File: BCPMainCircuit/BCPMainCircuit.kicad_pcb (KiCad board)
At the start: 2 copper layers, 94 x 88 mm, 8 parts, among them SW1 SW_Nidec_CAS-120A1, U1 LD1117V33, U2 Pico 2, U3 DEV-13712, U6 BME280

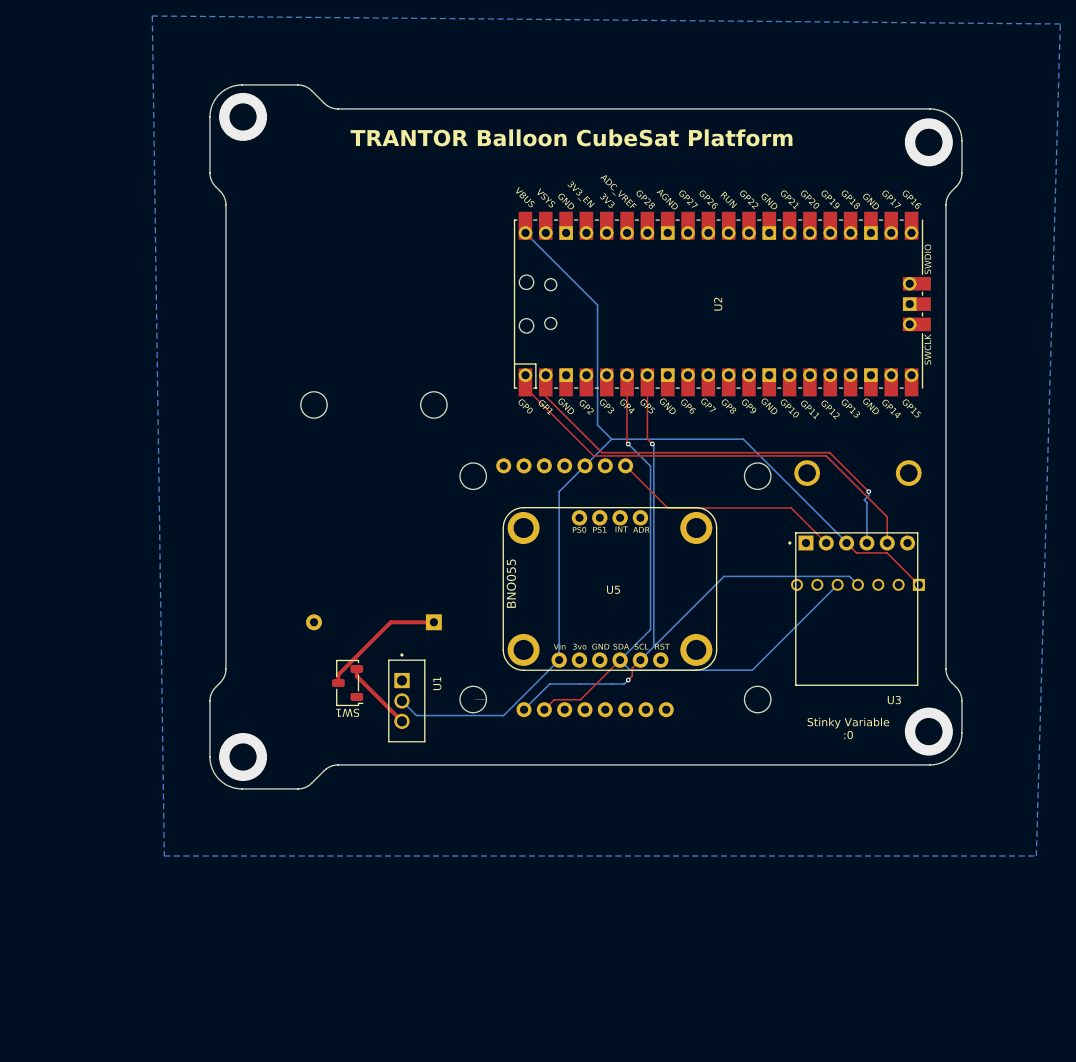
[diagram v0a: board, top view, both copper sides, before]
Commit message: Added a ground pour
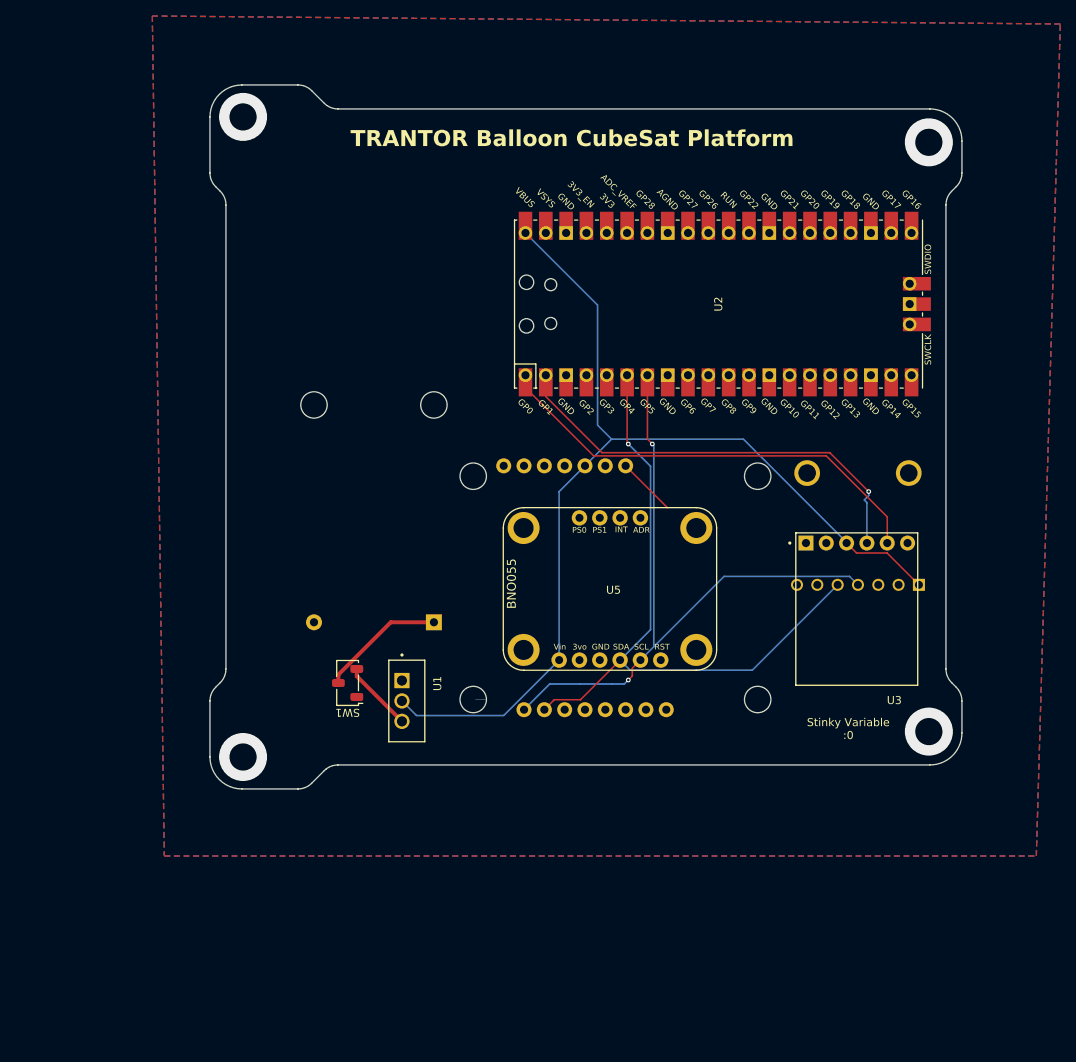
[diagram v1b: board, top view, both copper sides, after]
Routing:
- net GND: track 29.1 -> 7.45 mm
- added copper zone on F.Cu, net GND
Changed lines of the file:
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@@
-	)
-	(segment
-		(start 146.865 85)
-		(end 131.433372 85)
-		(width 0.2)
-		(layer "F.Cu")
-		(net 4)
 	)
 	(segment
 		(start 131.433372 85)
 		(end 126.162972 79.7296)
-		(width 0.2)
-		(layer "F.Cu")
-		(net 4)
-	)
-	(segment
-		(start 151.245 89.38)
-		(end 146.865 85)
 		(width 0.2)
 		(layer "F.Cu")
@@
 		(net 4)
 		(net_name "GND")
-		(layer "B.Cu")
+		(layers "F.Cu" "B.Cu")
 		(hatch edge 0.5)
 		(connect_pads

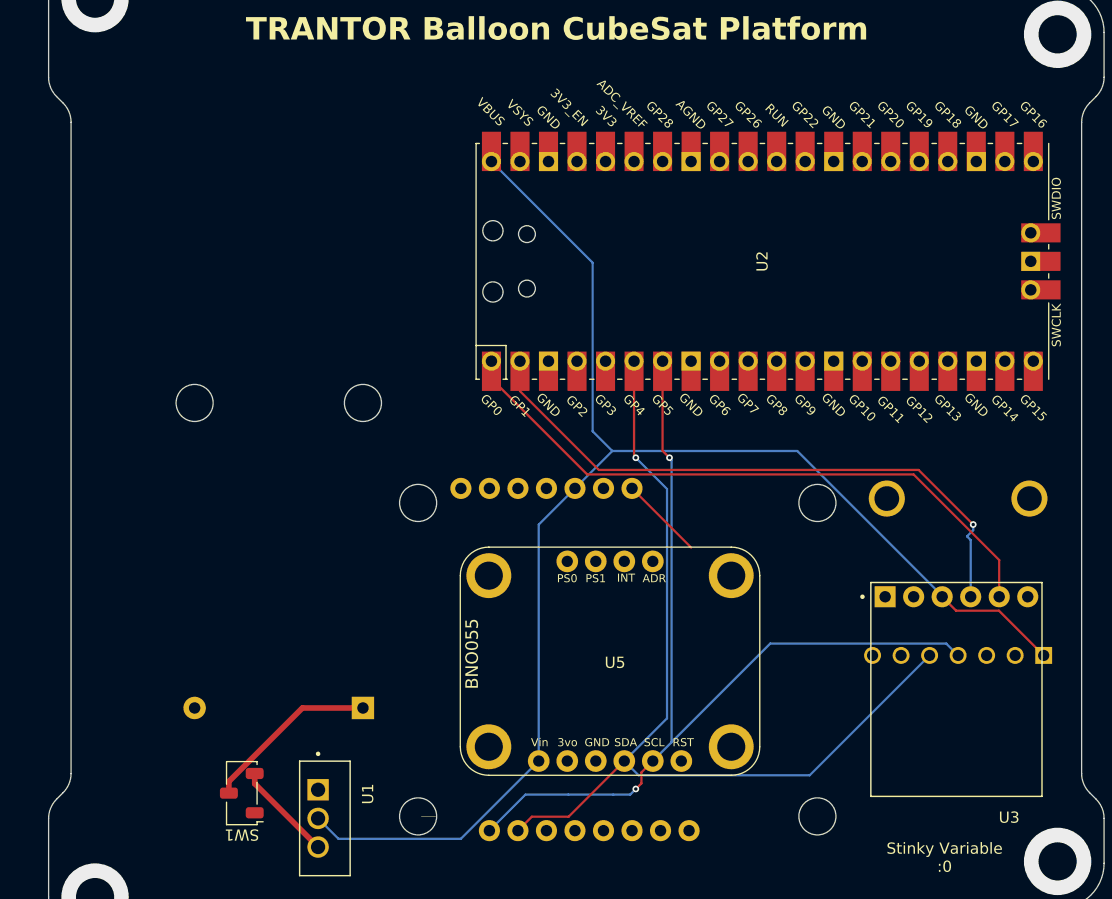
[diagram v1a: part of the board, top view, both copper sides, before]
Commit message: Fixed overlapping footprints
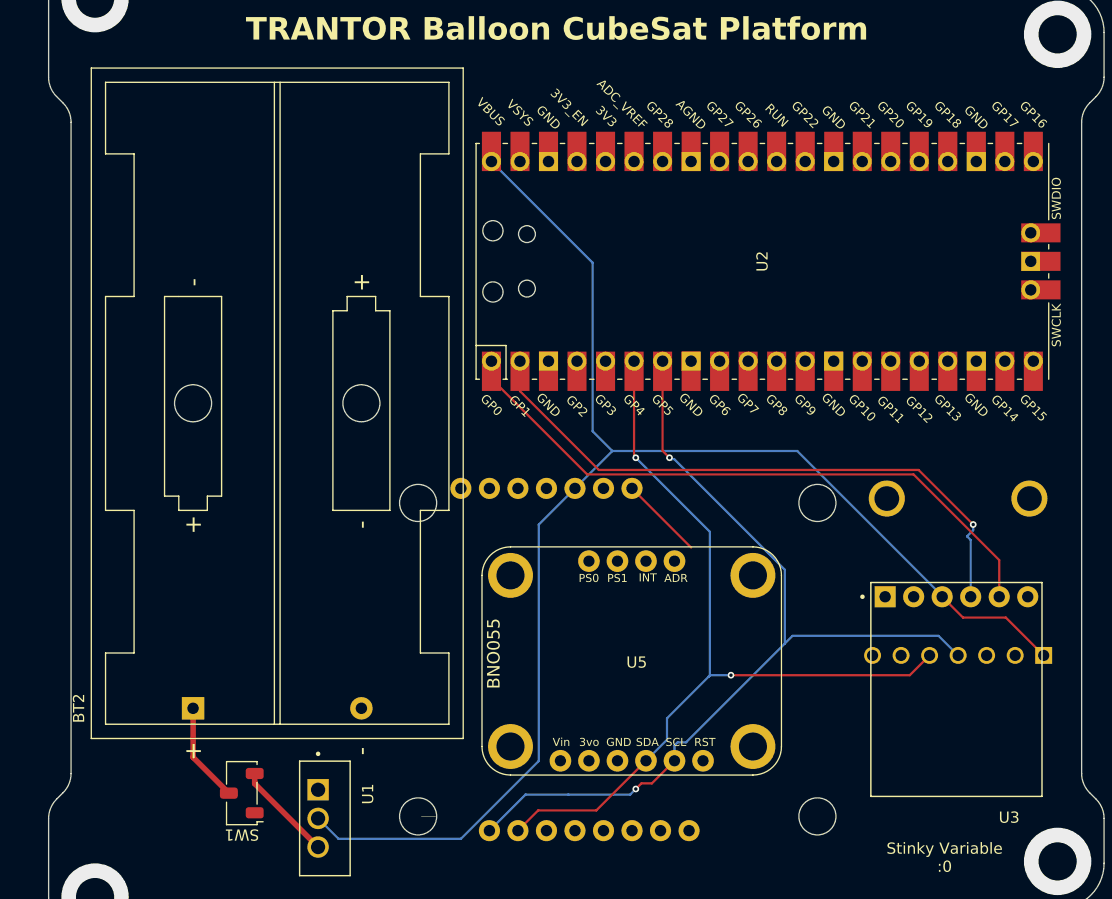
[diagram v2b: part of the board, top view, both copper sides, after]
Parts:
- BT2: moved to F.Cu
- moved BT2 15.1 mm to (87.1, 99.3)
- moved U5 1.93 mm to (126.6, 95.7)
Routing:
- net /SDA: track 82.6 -> 75.2 mm, vias 1 -> 2
- net Net-(BT2-+): track 15.7 -> 8.88 mm
- net /SCL: track 83.9 -> 80.2 mm

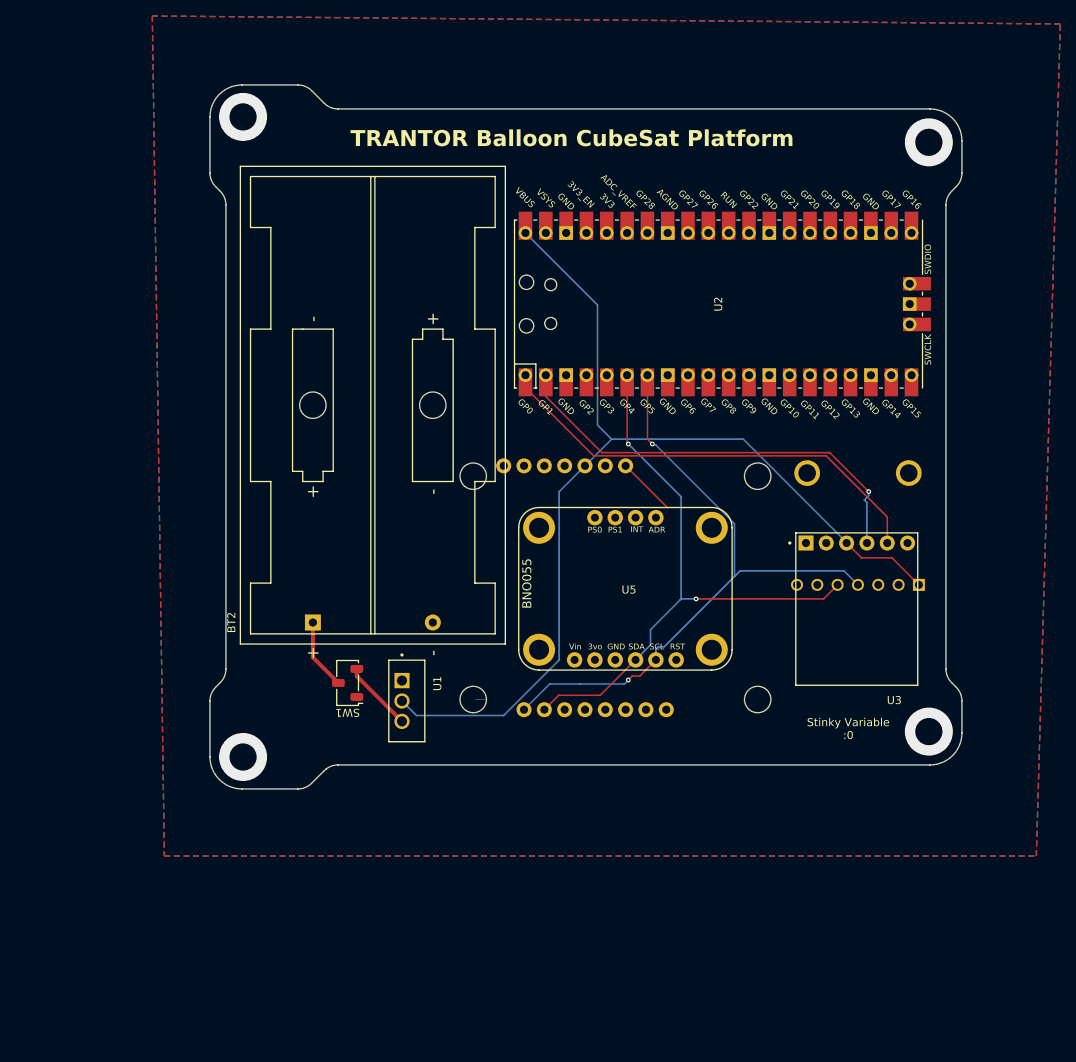
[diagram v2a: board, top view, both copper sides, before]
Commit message: Update LEDs and Silkscreen
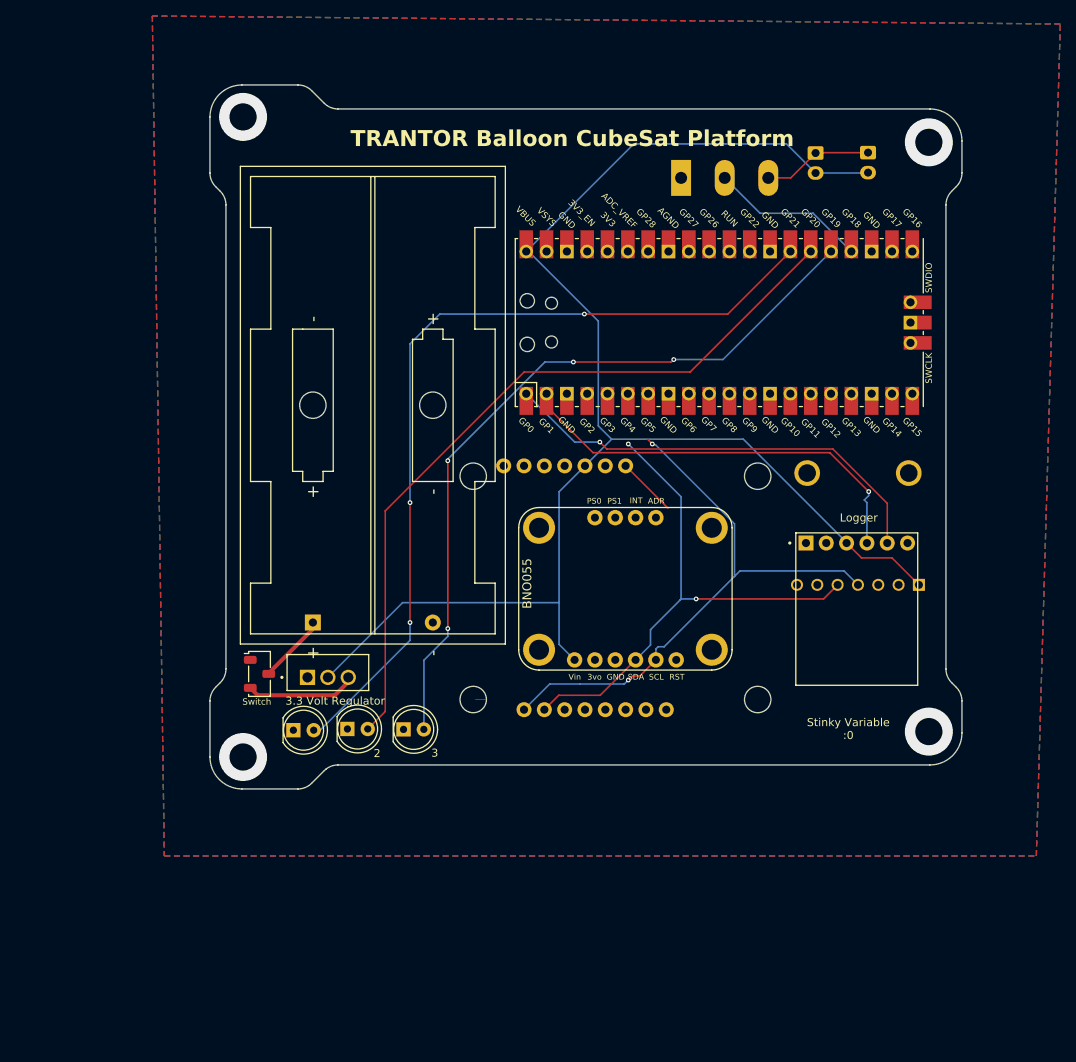
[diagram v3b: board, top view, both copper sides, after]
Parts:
- added D1: Flight LED 1, Connector_JST:JST_EH_B2B-EH-A_1x02_P2.50mm_Vertical, B.Cu at (156.5, 40.6)
- added D2: 1, LED_THT:LED_D5.0mm, F.Cu at (84.6, 112.8)
- added D3: 2, LED_THT:LED_D5.0mm, F.Cu at (91.4, 112.6)
- added D4: 3, LED_THT:LED_D5.0mm, F.Cu at (98.4, 112.7)
- added D5: Flight LED 2, Connector_JST:JST_EH_B2B-EH-A_1x02_P2.50mm_Vertical, B.Cu at (149.9, 40.6)
- added Mosfet: PMOS, Package_TO_SOT_THT:TO-247-3_Vertical, B.Cu at (133.1, 43.7)
- BT2: value Battery -> Batteries
- SW1: value SW_Nidec_CAS-120A1 -> Switch
- U1: value LD1117V33 -> 3.3 Volt Regulator
- U3: value DEV-13712 -> Logger
- U5: value ~ -> BNO055
- moved SW1 11.1 mm to (80.4, 105.7), turned to 0 degrees
- moved U1 10.5 mm to (88.9, 105.6), turned to 0 degrees
- moved U2 2.32 mm to (137.9, 61.8)
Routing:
- net /DEBUG1: track 0.00 -> 106.1 mm, vias 0 -> 3
- net /DEBUG2: track 0.00 -> 94.8 mm
- net /DEBUG3: track 0.00 -> 93.7 mm, vias 0 -> 4
- net /3.3 V: track 129.8 -> 187.9 mm
- net /FLIGHTLED: track 0.00 -> 19.6 mm
- net Net-(D1-K): track 0.00 -> 13.8 mm
- net /SDA: track 75.2 -> 66.7 mm
- net /SCL: track 80.2 -> 72.2 mm
- net Net-(SW1-A): track 8.89 -> 13.9 mm
- net /MCURX: track 54.7 -> 53.0 mm
- net /MCUTX: track 56.7 -> 55.8 mm, vias 0 -> 1
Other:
- board text added: "GPS"

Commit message: Update PCB design
Added four new backup ZIP files for BCPMainCircuit. Updated the KiCad PCB file to include a detailed stackup and new F.SilkS graphics, and made related changes to the .kicad_prl and fp-info-cache files.
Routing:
- net /SDA: track 66.7 -> 72.8 mm
- net /SCL: track 72.2 -> 77.8 mm

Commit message: added text
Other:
- board text added: "sea monkeys when?"
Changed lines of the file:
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@@
 		(layer "Edge.Cuts")
+	)
+	(gr_text "sea monkeys when?"
+		(at 135.25 115.25 0)
+		(layer "F.SilkS")
+		(effects
+			(font
+				(size 1 1)
+				(thickness 0.1)
+			)
+			(justify left bottom)
+		)
 	)
 	(gr_text "Stinky Variable\n:0"
